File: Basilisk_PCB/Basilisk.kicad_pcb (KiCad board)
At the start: 2 copper layers, 77 x 95 mm, 71 parts, among them J1 HUB75E, J2 Conn_01x04, J3 Barrel_Jack, J4 USB_C_Receptacle_USB2.0, Q1 S8050, Q2 S8050, SW1 IO0, SW2 RST, U1 AT25SF081-SSHD-X, U2 ESP32-WROOM-32D, U3 MLX90640, U4 TXS0108EPW, U5 TXS0108EPW, U6 AMS1117-3.3, U7 TPS54560BDDA, U8 FT231XS

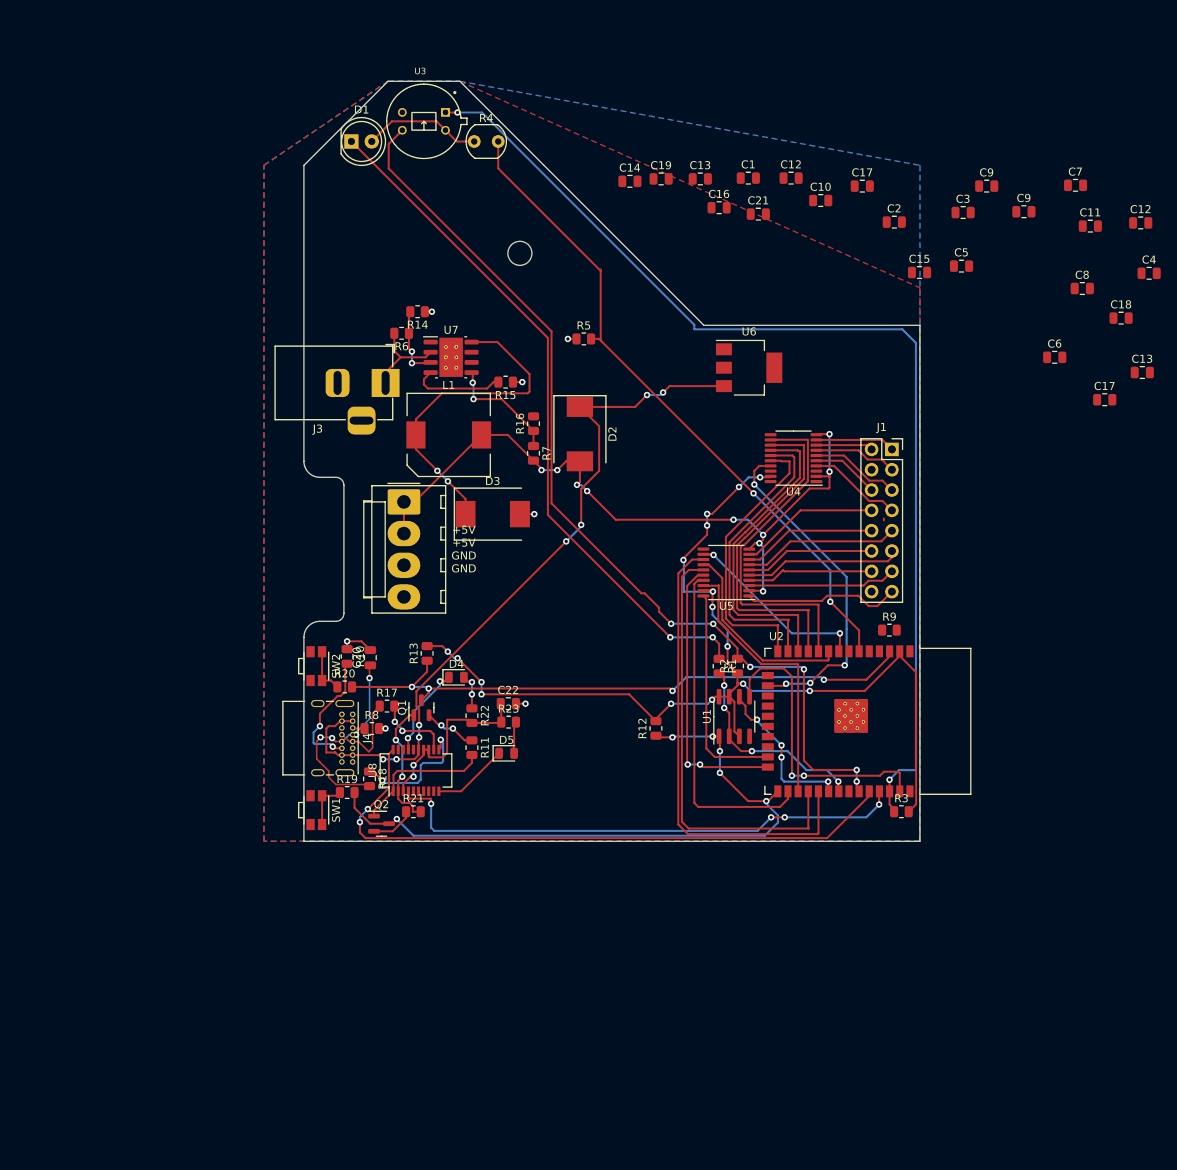
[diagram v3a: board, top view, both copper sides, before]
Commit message: almost done routuing
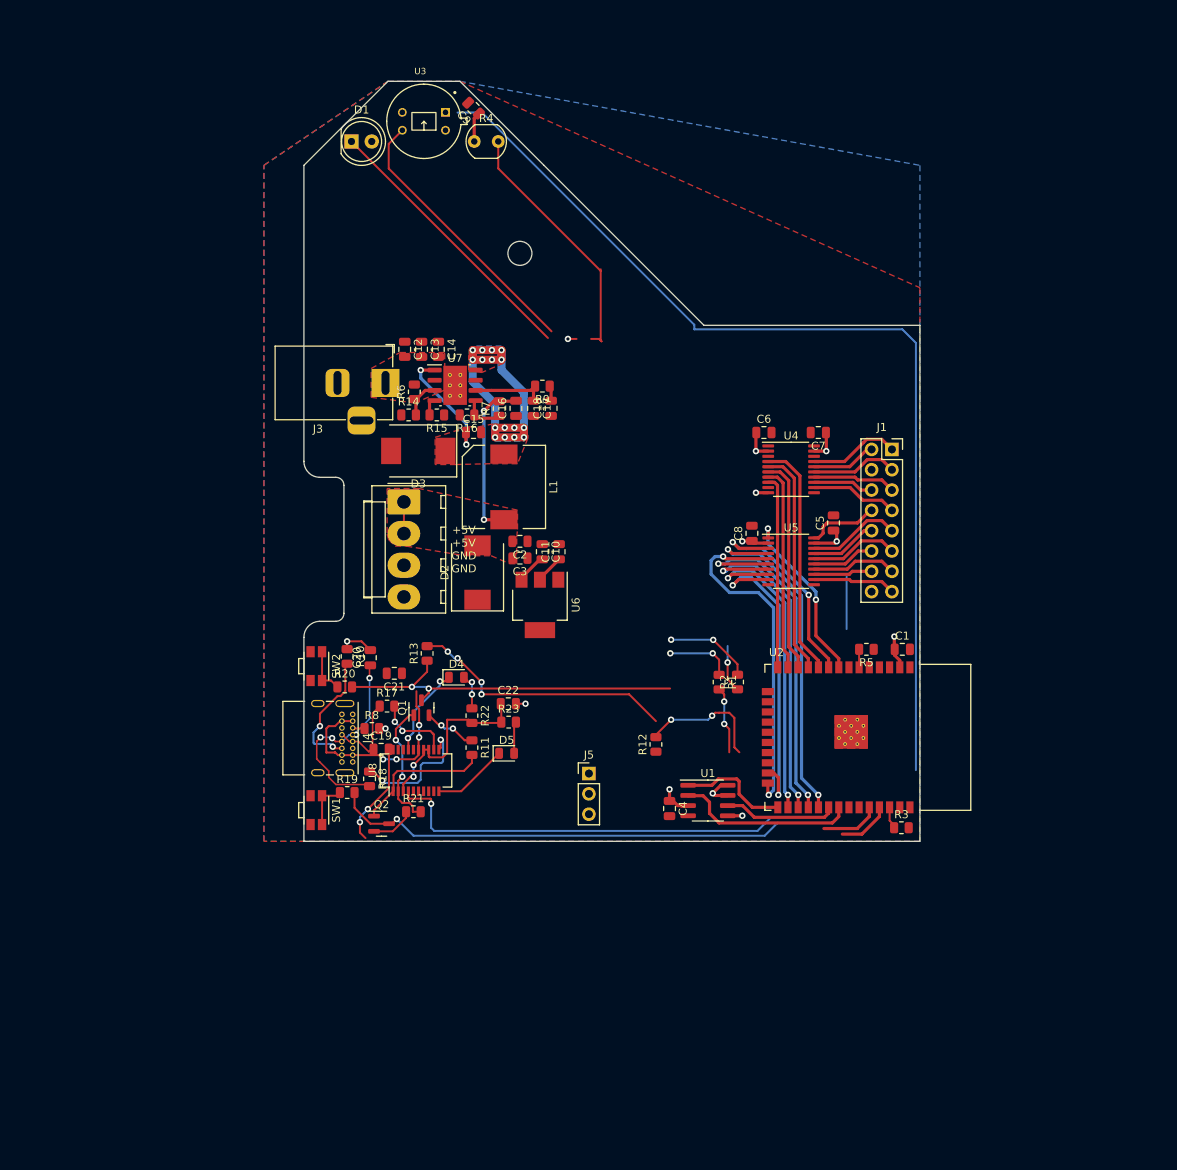
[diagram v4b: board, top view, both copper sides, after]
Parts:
- removed the C12 at (220.6, 34.2)
- removed the C13 at (220.8, 52.9)
- removed the C17 at (185.8, 29.6)
- removed the C9 at (206.0, 32.8)
- added J5: PRGM, Connector_PinHeader_2.54mm:PinHeader_1x03_P2.54mm_Vertical, F.Cu at (151.6, 103.0)
- moved C4 89.8 mm to (161.7, 107.4), turned to -90 degrees
- moved C19 79.4 mm to (125.7, 100.0)
- moved C11 77.9 mm to (147.9, 75.3), turned to 90 degrees
- moved C21 73.2 mm to (127.3, 90.5), turned to 180 degrees
- moved C18 72.1 mm to (146.9, 57.4), turned to 90 degrees
- moved C17 71.4 mm to (144.7, 57.4), turned to -90 degrees
- moved C3 70.3 mm to (143.0, 76.1), turned to 180 degrees
- moved C9 64.9 mm to (137.2, 19.9), turned to 135 degrees
- moved C1 62.0 mm to (190.8, 87.5)
- moved C2 61.5 mm to (143.0, 74.0), turned to 180 degrees
- moved C15 59.2 mm to (137.2, 60.4)
- moved C10 56.0 mm to (145.8, 75.3), turned to -90 degrees
- moved R9 53.0 mm to (145.8, 54.6), turned to 180 degrees
- moved C12 52.8 mm to (128.6, 50.0), turned to -90 degrees
- moved R5 52.5 mm to (186.3, 87.5), turned to 180 degrees
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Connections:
- U4 pad 10: +5V -> +3.3V
- U4 pad 12: /R1.3 -> /B2.5
- U4 pad 13: /G1.3 -> /G2.5
- U4 pad 14: /B1.3 -> /R2.5
- U4 pad 15: /R2.3 -> /B1.5
- U4 pad 16: /G2.3 -> /G1.5
- U4 pad 17: /B2.3 -> /R1.5
- U4 pad 19: +3.3V -> +5V
- U4 pad 2: +5V -> +3.3V
- U4 pad 4: /B2.5 -> /R1.3
- U4 pad 5: /G2.5 -> /G1.3
- U4 pad 6: /R2.5 -> /B1.3
- U4 pad 7: /B1.5 -> /R2.3
- U4 pad 8: /G1.5 -> /G2.3
- U4 pad 9: /R1.5 -> /B2.3
- U5 pad 1: /OE.5 -> /E.3
- U5 pad 10: +5V -> +3.3V
- U5 pad 12: /E.3 -> /OE.5
- U5 pad 13: /B.3 -> /LAT.5
- U5 pad 14: /A.3 -> /CLK.5
- U5 pad 15: /D.3 -> /D.5
- U5 pad 16: /C.3 -> /C.5
- U5 pad 17: /LAT.3 -> /B.5
- U5 pad 18: /CLK.3 -> /A.5
- U5 pad 19: +3.3V -> +5V
- U5 pad 2: +5V -> +3.3V
- U5 pad 20: /OE.3 -> /E.5
- U5 pad 3: /CLK.5 -> /A.3
- U5 pad 4: /LAT.5 -> /B.3
- U5 pad 5: /C.5 -> /C.3
- U5 pad 6: /D.5 -> /D.3
- U5 pad 7: /A.5 -> /CLK.3
- U5 pad 8: /B.5 -> /LAT.3
- U5 pad 9: /E.5 -> /OE.3
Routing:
- net /SDA: track 118.3 -> 45.2 mm, vias 6 -> 2
- net +3.3V: track 149.6 -> 84.9 mm, vias 16 -> 13
- net VBUS: track 92.0 -> 30.8 mm, vias 8 -> 4
- net +5V: track 92.3 -> 34.3 mm, vias 10 -> 4
- net /USB>ESP: track 78.8 -> 21.1 mm
- net Net-(U2-IO34): track 84.0 -> 34.6 mm, vias 2 -> 0
- net Net-(D1-K): track 86.8 -> 43.1 mm
- net /B2.3: track 42.1 -> 6.52 mm, vias 4 -> 0
- net /MOSI: track 36.9 -> 1.83 mm, vias 2 -> 1
- net /EN: track 75.2 -> 45.7 mm, vias 4 -> 2
- net Net-(U7-BOOT): track 0.00 -> 14.9 mm, vias 0 -> 2
- net /B.3: track 58.5 -> 44.2 mm, vias 0 -> 2
- net /R1.3: track 44.3 -> 30.1 mm
- net /G1.3: track 42.2 -> 28.7 mm
- net /B1.3: track 39.9 -> 26.8 mm
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- added copper zone on F.Cu, net +12V
- added copper zone on F.Cu, net +5V
- added copper zone on B.Cu, net Net-(D3-K)
- added copper zone on F.Cu, net Net-(D3-K)
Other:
- board text added: "locked"
- board text removed: "For Instructional Use Only."
- board text removed: "SOLIDWORKS Educational Product."

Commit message: version 1.0
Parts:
- added REF**: Fiducial_1mm_Mask2mm, Fiducial:Fiducial_1mm_Mask2mm, F.Cu at (131.0, 109.5)
- added REF**: Fiducial_1mm_Mask2mm, Fiducial:Fiducial_1mm_Mask2mm, F.Cu at (123.0, 51.5)
- added REF**: Fiducial_1mm_Mask2mm, Fiducial:Fiducial_1mm_Mask2mm, F.Cu at (188.0, 51.5)
- added REF**: Fiducial_1mm_Mask2mm, Fiducial:Fiducial_1mm_Mask2mm, F.Cu at (156.0, 81.5)
- added REF**: L_Wuerth_HCM-7070, Inductor_SMD:L_Wuerth_HCM-7070, F.Cu at (141.0, 67.2)
- moved Q2 24.6 mm to (143.8, 92.7), turned to -90 degrees
- moved R2 22.1 mm to (184.7, 108.3), turned to 0 degrees
- moved R12 19.7 mm to (142.8, 89.7), turned to 180 degrees
- moved R13 19.0 mm to (142.9, 103.1), turned to 180 degrees
- moved R21 18.9 mm to (144.8, 96.4), turned to -90 degrees
- moved R10 16.6 mm to (121.3, 105.0), turned to 180 degrees
- moved Q1 14.1 mm to (143.8, 100.1)
- moved R1 11.6 mm to (161.4, 101.2)
- moved C21 11.1 mm to (133.9, 99.4), turned to 0 degrees
- moved U8 10.7 mm to (134.8, 93.1), turned to -90 degrees
- moved D4 10.4 mm to (136.7, 101.3), turned to -90 degrees
- moved R22 9.02 mm to (136.7, 104.8)
- moved C22 8.84 mm to (135.2, 88.2), turned to 180 degrees
- moved R23 8.66 mm to (138.8, 104.8), turned to 90 degrees
- moved C20 8.30 mm to (124.3, 96.8)
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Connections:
- J3 pad 3: (no net) -> GND
- Q1 pad 1: /RTS -> Net-(Q1-B)
- Q1 pad 2: Net-(Q1-B) -> /RTS
- Q2 pad 1: /DTR -> Net-(Q2-B)
- Q2 pad 2: Net-(Q2-B) -> /DTR
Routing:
- net Net-(D1-K): track 43.1 -> 147.0 mm, vias 2 -> 3
- net /SDA: track 45.2 -> 129.9 mm, vias 2 -> 1
- net /EN: track 45.7 -> 107.2 mm, vias 2 -> 3
- net +5V: track 34.3 -> 87.7 mm
- net Net-(U2-IO34): track 34.6 -> 87.1 mm, vias 0 -> 1
- net /USB>ESP: track 21.1 -> 62.5 mm, vias 2 -> 1
- net /B2.3: track 6.52 -> 42.1 mm, vias 0 -> 2
- net +3.3V: track 84.9 -> 60.0 mm, vias 13 -> 20
- net /MOSI: track 1.83 -> 25.5 mm, vias 1 -> 2
- net /D+: track 25.8 -> 6.03 mm, vias 4 -> 0
- net /CMD: track 71.4 -> 90.1 mm, vias 1 -> 4
- net /ESP>USB: track 57.4 -> 71.8 mm
- net VBUS: track 30.8 -> 19.3 mm, vias 4 -> 9
- net Net-(U8-USBDP): track 16.3 -> 5.37 mm, vias 2 -> 0
- net Net-(J4-CC2): track 15.8 -> 6.72 mm, vias 2 -> 0
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- added copper zone on F.Cu, net +3.3V
- added copper zone on B.Cu, net VBUS
- added copper zone on F.Cu, net VBUS
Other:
- outline, holes or cut-outs redrawn
- board text added: "ANHAD SAWHNEY JUAN ALVAREZ KAT JANDER PRESENT"
- board text added: "ESP: TX ESP: RX GND"
- board text added: "G1 GND G2 E B D LAT GND"
- board text added: "R1 B1 R2 B2 A C CLK ~{OE}"
- board text added: "V1.0"

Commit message: start solidworks cad
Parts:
- renumbered R4 to Ree
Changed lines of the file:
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@@
     (pad "2" smd roundrect (at 3.4 0 180) (size 3.3 2.5) (layers "F.Cu" "F.Paste" "F.Mask") (roundrect_rratio 0.1)
       (net 4 "+5V") (pinfunction "A") (pintype "passive"))
-    (model "${KICAD6_3DMODEL_DIR}/Diode_SMD.3dshapes/D_SMC.wrl"
+    (model "${KICAD6_3DMODEL_DIR}/Diode_SMD.3dshapes/D_SMC.step"
       (offset (xyz 0 0 0))
       (scale (xyz 1 1 1))
@@
     (pad "20" smd roundrect locked (at 2.8625 -2.925) (size 1.475 0.4) (layers "F.Cu" "F.Paste" "F.Mask") (roundrect_rratio 0.25)
       (net 22 "/E.5") (pinfunction "B1") (pintype "bidirectional"))
-    (model "${KICAD6_3DMODEL_DIR}/Package_SO.3dshapes/TSSOP-20_4.4x6.5mm_P0.65mm.wrl"
+    (model "${KICAD6_3DMODEL_DIR}/Package_SO.3dshapes/TSSOP-20_4.4x6.5mm_P0.65mm.step"
       (offset (xyz 0 0 0))
       (scale (xyz 1 1 1))
@@
     (pad "20" smd roundrect locked (at 2.8625 -2.925) (size 1.475 0.4) (layers "F.Cu" "F.Paste" "F.Mask") (roundrect_rratio 0.25)
       (net 83 "unconnected-(U4-B1-Pad20)") (pinfunction "B1") (pintype "bidirectional+no_connect"))
-    (model "${KICAD6_3DMODEL_DIR}/Package_SO.3dshapes/TSSOP-20_4.4x6.5mm_P0.65mm.wrl"
+    (model "${KICAD6_3DMODEL_DIR}/Package_SO.3dshapes/TSSOP-20_4.4x6.5mm_P0.65mm.step"
       (offset (xyz 0 0 0))
       (scale (xyz 1 1 1))
@@
       (rotate (xyz 0 0 0))
     )
+    (model "${KIPRJMOD}/3D/WE-PDF_1064 (rev1).stp"
+      (offset (xyz 0 0 0))
+      (scale (xyz 1 1 1))
+      (rotate (xyz 0 0 90))
+    )
   )
   (footprint "Capacitor_SMD:C_0805_2012Metric" (layer "F.Cu")
@@
     (pad "2" thru_hole circle locked (at 2.54 0 180) (size 1.8 1.8) (drill 0.9) (layers "*.Cu" "*.Mask")
       (net 1 "+3.3V") (pinfunction "A") (pintype "passive"))
-    (model "${KICAD6_3DMODEL_DIR}/LED_THT.3dshapes/LED_D5.0mm_Clear.wrl"
-      (offset (xyz 0 0 0))
+    (model "${KICAD6_3DMODEL_DIR}/LED_THT.3dshapes/LED_D5.0mm_Clear.step"
+      (offset (xyz 0 0 -3))
       (scale (xyz 1 1 1))
       (rotate (xyz 0 0 0))
@@
       (rotate (xyz 0 0 0))
     )
+    (model "${KIPRJMOD}/3D/USB4085-GF-A.stp"
+      (offset (xyz 15 -4 1.8))
+      (scale (xyz 1 1 1))
+      (rotate (xyz -90 0 0))
+    )
   )
   (footprint "Resistor_SMD:R_0805_2012Metric" (layer "F.Cu")
@@
     (pad "8" smd roundrect (at 2.475 -1.905) (size 1.95 0.6) (layers "F.Cu" "F.Paste" "F.Mask") (roundrect_rratio 0.25)
       (net 1 "+3.3V") (pinfunction "VCC") (pintype "power_in"))
-    (model "${KICAD6_3DMODEL_DIR}/Package_SO.3dshapes/SOIC-8_3.9x4.9mm_P1.27mm.wrl"
+    (model "${KICAD6_3DMODEL_DIR}/Package_SO.3dshapes/SOIC-8_3.9x4.9mm_P1.27mm.step"
       (offset (xyz 0 0 0))
       (scale (xyz 1 1 1))
@@
       (rotate (xyz 0 0 0))
     )
+    (model ":KICAD7_3DMODEL_DIR:Package_SO.3dshapes/SOIC-8-1EP_3.9x4.9mm_P1.27mm_EP2.35x2.35mm.step"
+      (offset (xyz 0 0 0))
+      (scale (xyz 1 1 1))
+      (rotate (xyz 0 0 0))
+    )
   )
   (footprint "Package_TO_SOT_SMD:SOT-223-3_TabPin2" (layer "F.Cu")
@@
     (pad "3" smd rect (at -3.15 2.3 270) (size 2 1.5) (layers "F.Cu" "F.Paste" "F.Mask")
       (net 8 "VBUS") (pinfunction "VI") (pintype "power_in"))
-    (model "${KICAD6_3DMODEL_DIR}/Package_TO_SOT_SMD.3dshapes/SOT-223.wrl"
+    (model "${KICAD6_3DMODEL_DIR}/Package_TO_SOT_SMD.3dshapes/SOT-223.step"
       (offset (xyz 0 0 0))
       (scale (xyz 1 1 1))
@@
       (rotate (xyz 0 0 0))
     )
+    (model "${KIPRJMOD}/3D/DS-210.step"
+      (offset (xyz -13.75 0 0))
+      (scale (xyz 1 1 1))
+      (rotate (xyz 0 0 -90))
+    )
   )
   (footprint "Resistor_SMD:R_0805_2012Metric" (layer "F.Cu")
@@
         (effects (font (size 1 1) (thickness 0.15)))
     )
-    (fp_text value "RST" (at 0 -0.15 -90) (layer "B.SilkS")
+    (fp_text value "RST" (at 0 -0.15 90) (layer "B.SilkS")
         (effects (font (size 1 1) (thickness 0.15)) (justify mirror))
     )
@@
       (rotate (xyz 0 0 0))
     )
+    (model "${KIPRJMOD}/3D/EVQP7-JA-01P.STEP"
+      (offset (xyz 0 0 0))
+      (scale (xyz 1 1 1))
+      (rotate (xyz -90 0 0))
+    )
   )
   (footprint "OptoDevice:R_LDR_5.0x4.1mm_P3mm_Vertical" locked (layer "F.Cu")
@@
     (property "ki_keywords" "light dependent photo resistor LDR")
     (attr through_hole)
-    (fp_text reference "R4" (at 1.5 -2.9) (layer "F.SilkS") hide
+    (fp_text reference "Ree" (at 1.5 -2.9) (layer "F.SilkS") hide
         (effects (font (size 1 1) (thickness 0.15)))
     )
@@
     (pad "2" thru_hole circle locked (at 3 0) (size 1.6 1.6) (drill 0.8) (layers "*.Cu" "*.Mask")
       (net 42 "Net-(U2-IO34)") (pintype "passive"))
-    (model "${KICAD6_3DMODEL_DIR}/OptoDevice.3dshapes/R_LDR_5.0x4.1mm_P3mm_Vertical.wrl"
+    (model "${KICAD6_3DMODEL_DIR}/OptoDevice.3dshapes/R_LDR_5.0x4.1mm_P3mm_Vertical.step"
       (offset (xyz 0 0 0))
       (scale (xyz 1 1 1))
@@
     (pad "20" smd rect (at 2.6 -2.8575 270) (size 1.2 0.4) (layers "F.Cu" "F.Paste" "F.Mask")
       (net 77 "/USB>ESP") (pinfunction "TXD") (pintype "output"))
-    (model "${KICAD6_3DMODEL_DIR}/Package_SO.3dshapes/SSOP-20_3.9x8.7mm_P0.635mm.wrl"
+    (model "${KICAD6_3DMODEL_DIR}/Package_SO.3dshapes/SSOP-20_3.9x8.7mm_P0.635mm.step"
       (offset (xyz 0 0 0))
       (scale (xyz 1 1 1))
@@
       (rotate (xyz 0 0 0))
     )
+    (model "${KIPRJMOD}/3D/EVQP7-JA-01P.STEP"
+      (offset (xyz 0 0 0))
+      (scale (xyz 1 1 1))
+      (rotate (xyz -90 0 0))
+    )
   )
   (footprint "basilisk:TO292P930H600-4" locked (layer "F.Cu")
@@
     (pad "4" smd roundrect locked (at 1.117436 -2.697728 90) (size 2.41 1.75) (layers "B.Cu" "B.Paste" "B.Mask") (roundrect_rratio 0.25)
       (net 1 "+3.3V") (pinfunction "VCC") (pintype "power_in"))
+    (model "${KIPRJMOD}/3D/MLX90640.STEP"
+      (offset (xyz 0 0 6))
+      (scale (xyz 1 1 1))
+      (rotate (xyz -90 0 -112.5))
+    )
   )
   (footprint "Package_TO_SOT_SMD:SOT-23" (layer "F.Cu")
@@
       )
     )
-    (model "${KICAD6_3DMODEL_DIR}/RF_Module.3dshapes/ESP32-WROOM-32.wrl"
+    (model "${KICAD6_3DMODEL_DIR}/RF_Module.3dshapes/ESP32-WROOM-32.step"
       (offset (xyz 0 0 0))
       (scale (xyz 1 1 1))
@@
     (pad "2" smd roundrect (at 3.4 0 270) (size 3.3 2.5) (layers "F.Cu" "F.Paste" "F.Mask") (roundrect_rratio 0.1)
       (net 2 "GND") (pinfunction "A") (pintype "passive"))
-    (model "${KICAD6_3DMODEL_DIR}/Diode_SMD.3dshapes/D_SMC.wrl"
+    (model "${KICAD6_3DMODEL_DIR}/Diode_SMD.3dshapes/D_SMC.step"
       (offset (xyz 0 0 0))
       (scale (xyz 1 1 1))
@@
     (pad "16" thru_hole oval locked (at -2.54 17.78) (size 1.7 1.7) (drill 1) (layers "*.Cu" "*.Mask")
       (net 2 "GND") (pinfunction "Pin_16") (pintype "passive"))
-    (model "${KICAD6_3DMODEL_DIR}/Connector_PinSocket_2.54mm.3dshapes/PinSocket_2x08_P2.54mm_Vertical.wrl"
+    (model "${KICAD6_3DMODEL_DIR}/Connector_PinSocket_2.54mm.3dshapes/PinSocket_2x08_P2.54mm_Vertical.step"
       (offset (xyz 0 0 0))
       (scale (xyz 1 1 1))
